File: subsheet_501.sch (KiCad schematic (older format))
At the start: 11 parts, among them P500 4K7 ×8, P501 4K7 ×8, P502 4K7 ×8, U509 74LS244_PHY, U510 74LS244_PHY, U511 74LS373_PHY, U512 74LS244_PHY

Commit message: Resolves #1 : Use 4-resistor packs wherever it is possible
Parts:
- removed P500, P501, P502: 4K7 ×8, Resistor_THT:R_Array_SIP9, symbol Device:R_Network08_US
- added RN? (x6): 4K7 ×4, symbol custom_passives:R_Pack04_US
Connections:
- wire segments 115 -> 160

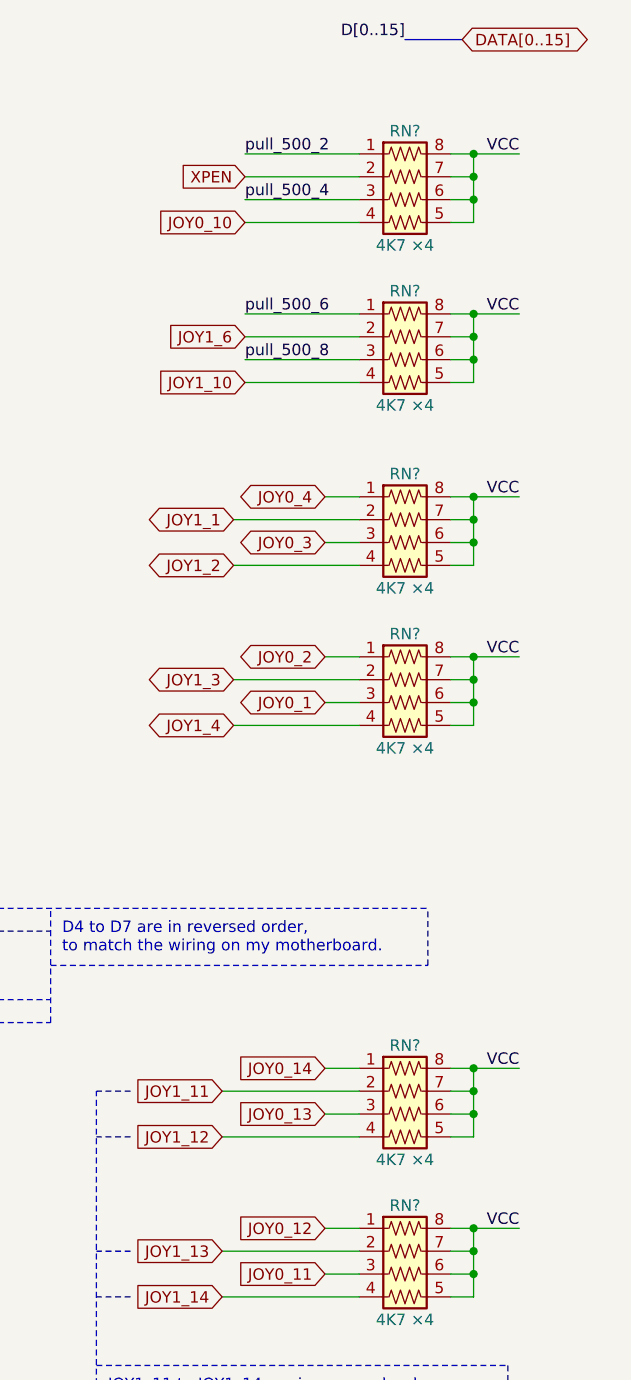
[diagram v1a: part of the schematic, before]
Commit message: annotate resistor networks and mark unused pins as unconnected
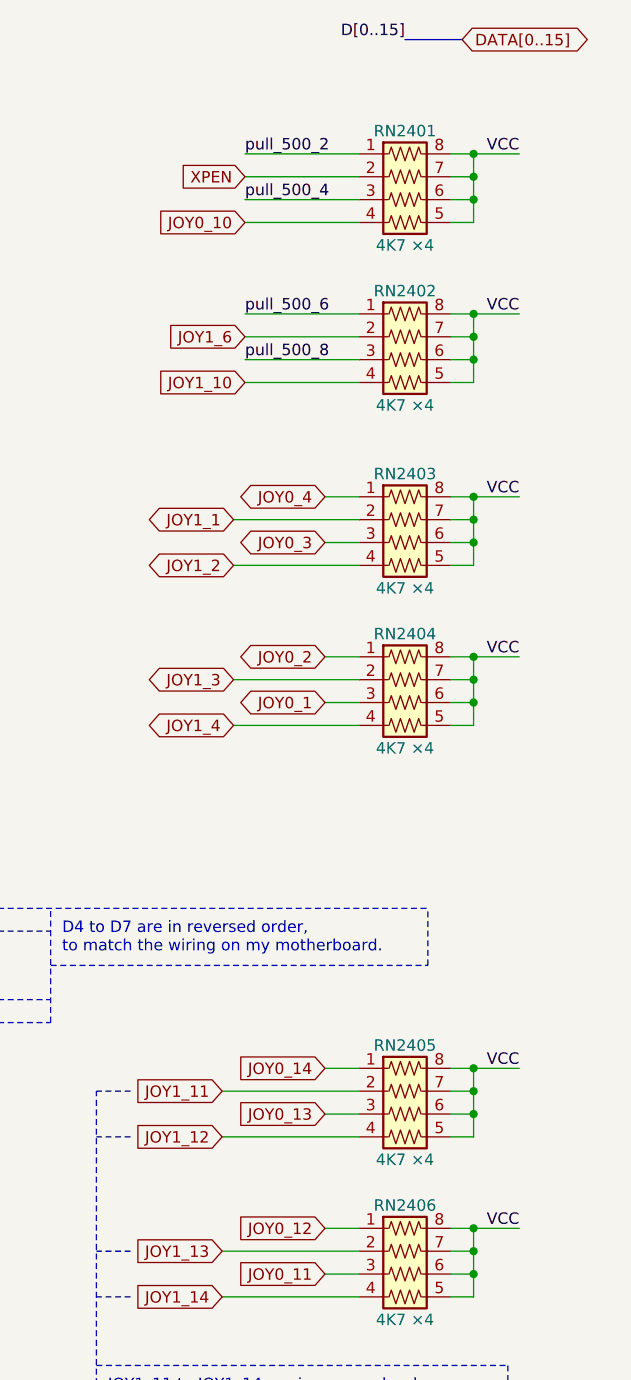
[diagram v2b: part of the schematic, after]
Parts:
- gave numbers to parts that had none: 6
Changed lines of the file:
@@
 	4300 5300 4950 5300
 $Comp
-L custom_passives:R_Pack04_US RN?
+L custom_passives:R_Pack04_US RN2403
 U 1 1 624905E3
 P 6500 3200
-F 0 "RN?" V 6200 3200 50  0000 C CNN
+F 0 "RN2403" V 6200 3200 50  0000 C CNN
 F 1 "4K7 ×4" V 6700 3200 50  0000 C CNN
 F 2 "" V 6775 3200 50  0001 C CNN
@@
 	6800 3100 6800 3000
 $Comp
-L custom_passives:R_Pack04_US RN?
+L custom_passives:R_Pack04_US RN2404
 U 1 1 6249D1FA
 P 6500 3900
-F 0 "RN?" V 6200 3900 50  0000 C CNN
+F 0 "RN2404" V 6200 3900 50  0000 C CNN
 F 1 "4K7 ×4" V 6700 3900 50  0000 C CNN
 F 2 "" V 6775 3900 50  0001 C CNN
@@
 	4950 5300 4950 4800
 $Comp
-L custom_passives:R_Pack04_US RN?
+L custom_passives:R_Pack04_US RN2405
 U 1 1 624C36D6
 P 6500 5700
-F 0 "RN?" V 6200 5700 50  0000 C CNN
+F 0 "RN2405" V 6200 5700 50  0000 C CNN
 F 1 "4K7 ×4" V 6700 5700 50  0000 C CNN
 F 2 "" V 6775 5700 50  0001 C CNN
@@
 	6800 5600 6800 5500
 $Comp
-L custom_passives:R_Pack04_US RN?
+L custom_passives:R_Pack04_US RN2406
 U 1 1 624D7AF3
 P 6500 6400
-F 0 "RN?" V 6200 6400 50  0000 C CNN
+F 0 "RN2406" V 6200 6400 50  0000 C CNN
 F 1 "4K7 ×4" V 6700 6400 50  0000 C CNN
 F 2 "" V 6775 6400 50  0001 C CNN
@@
 	6800 6300 6800 6200
 $Comp
-L custom_passives:R_Pack04_US RN?
+L custom_passives:R_Pack04_US RN2402
 U 1 1 62508706
 P 6500 2400
-F 0 "RN?" V 6200 2400 50  0000 C CNN
+F 0 "RN2402" V 6200 2400 50  0000 C CNN
 F 1 "4K7 ×4" V 6700 2400 50  0000 C CNN
 F 2 "" V 6775 2400 50  0001 C CNN
@@
 	6800 2300 6800 2200
 $Comp
-L custom_passives:R_Pack04_US RN?
+L custom_passives:R_Pack04_US RN2401
 U 1 1 62529C81
 P 6500 1700
-F 0 "RN?" V 6200 1700 50  0000 C CNN
+F 0 "RN2401" V 6200 1700 50  0000 C CNN
 F 1 "4K7 ×4" V 6700 1700 50  0000 C CNN
 F 2 "" V 6775 1700 50  0001 C CNN

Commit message: Resolves #7 : Assign SMD footprints to resistors pack
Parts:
- RN2401, RN2402, RN2403, RN2404, RN2405, RN2406: footprint (none) -> Resistor_SMD:R_Array_Convex_4x0603
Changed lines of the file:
@@
 F 0 "RN2403" V 6200 3200 50  0000 C CNN
 F 1 "4K7 ×4" V 6700 3200 50  0000 C CNN
-F 2 "" V 6775 3200 50  0001 C CNN
+F 2 "Resistor_SMD:R_Array_Convex_4x0603" V 6775 3200 50  0001 C CNN
 F 3 "~" H 6500 3200 50  0001 C CNN
 	1    6500 3200
@@
 F 0 "RN2404" V 6200 3900 50  0000 C CNN
 F 1 "4K7 ×4" V 6700 3900 50  0000 C CNN
-F 2 "" V 6775 3900 50  0001 C CNN
+F 2 "Resistor_SMD:R_Array_Convex_4x0603" V 6775 3900 50  0001 C CNN
 F 3 "~" H 6500 3900 50  0001 C CNN
 	1    6500 3900
@@
 F 0 "RN2405" V 6200 5700 50  0000 C CNN
 F 1 "4K7 ×4" V 6700 5700 50  0000 C CNN
-F 2 "" V 6775 5700 50  0001 C CNN
+F 2 "Resistor_SMD:R_Array_Convex_4x0603" V 6775 5700 50  0001 C CNN
 F 3 "~" H 6500 5700 50  0001 C CNN
 	1    6500 5700
@@
 F 0 "RN2406" V 6200 6400 50  0000 C CNN
 F 1 "4K7 ×4" V 6700 6400 50  0000 C CNN
-F 2 "" V 6775 6400 50  0001 C CNN
+F 2 "Resistor_SMD:R_Array_Convex_4x0603" V 6775 6400 50  0001 C CNN
 F 3 "~" H 6500 6400 50  0001 C CNN
 	1    6500 6400
@@
 F 0 "RN2402" V 6200 2400 50  0000 C CNN
 F 1 "4K7 ×4" V 6700 2400 50  0000 C CNN
-F 2 "" V 6775 2400 50  0001 C CNN
+F 2 "Resistor_SMD:R_Array_Convex_4x0603" V 6775 2400 50  0001 C CNN
 F 3 "~" H 6500 2400 50  0001 C CNN
 	1    6500 2400
@@
 F 0 "RN2401" V 6200 1700 50  0000 C CNN
 F 1 "4K7 ×4" V 6700 1700 50  0000 C CNN
-F 2 "" V 6775 1700 50  0001 C CNN
+F 2 "Resistor_SMD:R_Array_Convex_4x0603" V 6775 1700 50  0001 C CNN
 F 3 "~" H 6500 1700 50  0001 C CNN
 	1    6500 1700

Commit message: Resolves #8 : Assign 1206 hand-solder footprints to non polarized capacitors
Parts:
- C550, C551, C552, C553: footprint commons_passives_THT:Passive_THT_capacitor_mlcc_W2.54mm_L7.62mm -> Capacitor_SMD:C_1206_3216Metric_Pad1.33x1.80mm_HandSolder
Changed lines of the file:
@@
 F 0 "C553" H 1775 2350 50  0000 L CNN
 F 1 "0.1uF" H 1775 2150 50  0000 L CNN
-F 2 "commons_passives_THT:Passive_THT_capacitor_mlcc_W2.54mm_L7.62mm" H 1788 2100 50  0001 C CNN
+F 2 "Capacitor_SMD:C_1206_3216Metric_Pad1.33x1.80mm_HandSolder" H 1788 2100 50  0001 C CNN
 F 3 "~" H 1750 2250 50  0001 C CNN
 	1    1750 2250
@@
 F 0 "C551" H 1775 3850 50  0000 L CNN
 F 1 "0.1uF" H 1775 3650 50  0000 L CNN
-F 2 "commons_passives_THT:Passive_THT_capacitor_mlcc_W2.54mm_L7.62mm" H 1788 3600 50  0001 C CNN
+F 2 "Capacitor_SMD:C_1206_3216Metric_Pad1.33x1.80mm_HandSolder" H 1788 3600 50  0001 C CNN
 F 3 "~" H 1750 3750 50  0001 C CNN
 	1    1750 3750
@@
 F 0 "C552" H 1775 5350 50  0000 L CNN
 F 1 "0.1uF" H 1775 5150 50  0000 L CNN
-F 2 "commons_passives_THT:Passive_THT_capacitor_mlcc_W2.54mm_L7.62mm" H 1788 5100 50  0001 C CNN
+F 2 "Capacitor_SMD:C_1206_3216Metric_Pad1.33x1.80mm_HandSolder" H 1788 5100 50  0001 C CNN
 F 3 "~" H 1750 5250 50  0001 C CNN
 	1    1750 5250
@@
 F 0 "C550" H 1775 6850 50  0000 L CNN
 F 1 "0.1uF" H 1775 6650 50  0000 L CNN
-F 2 "commons_passives_THT:Passive_THT_capacitor_mlcc_W2.54mm_L7.62mm" H 1788 6600 50  0001 C CNN
+F 2 "Capacitor_SMD:C_1206_3216Metric_Pad1.33x1.80mm_HandSolder" H 1788 6600 50  0001 C CNN
 F 3 "~" H 1750 6750 50  0001 C CNN
 	1    1750 6750
